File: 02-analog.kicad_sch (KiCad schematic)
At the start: 24 parts, among them J2 Superseal_1.0_5pol_MicA, J3 Superseal_1.0_5pol_MicB

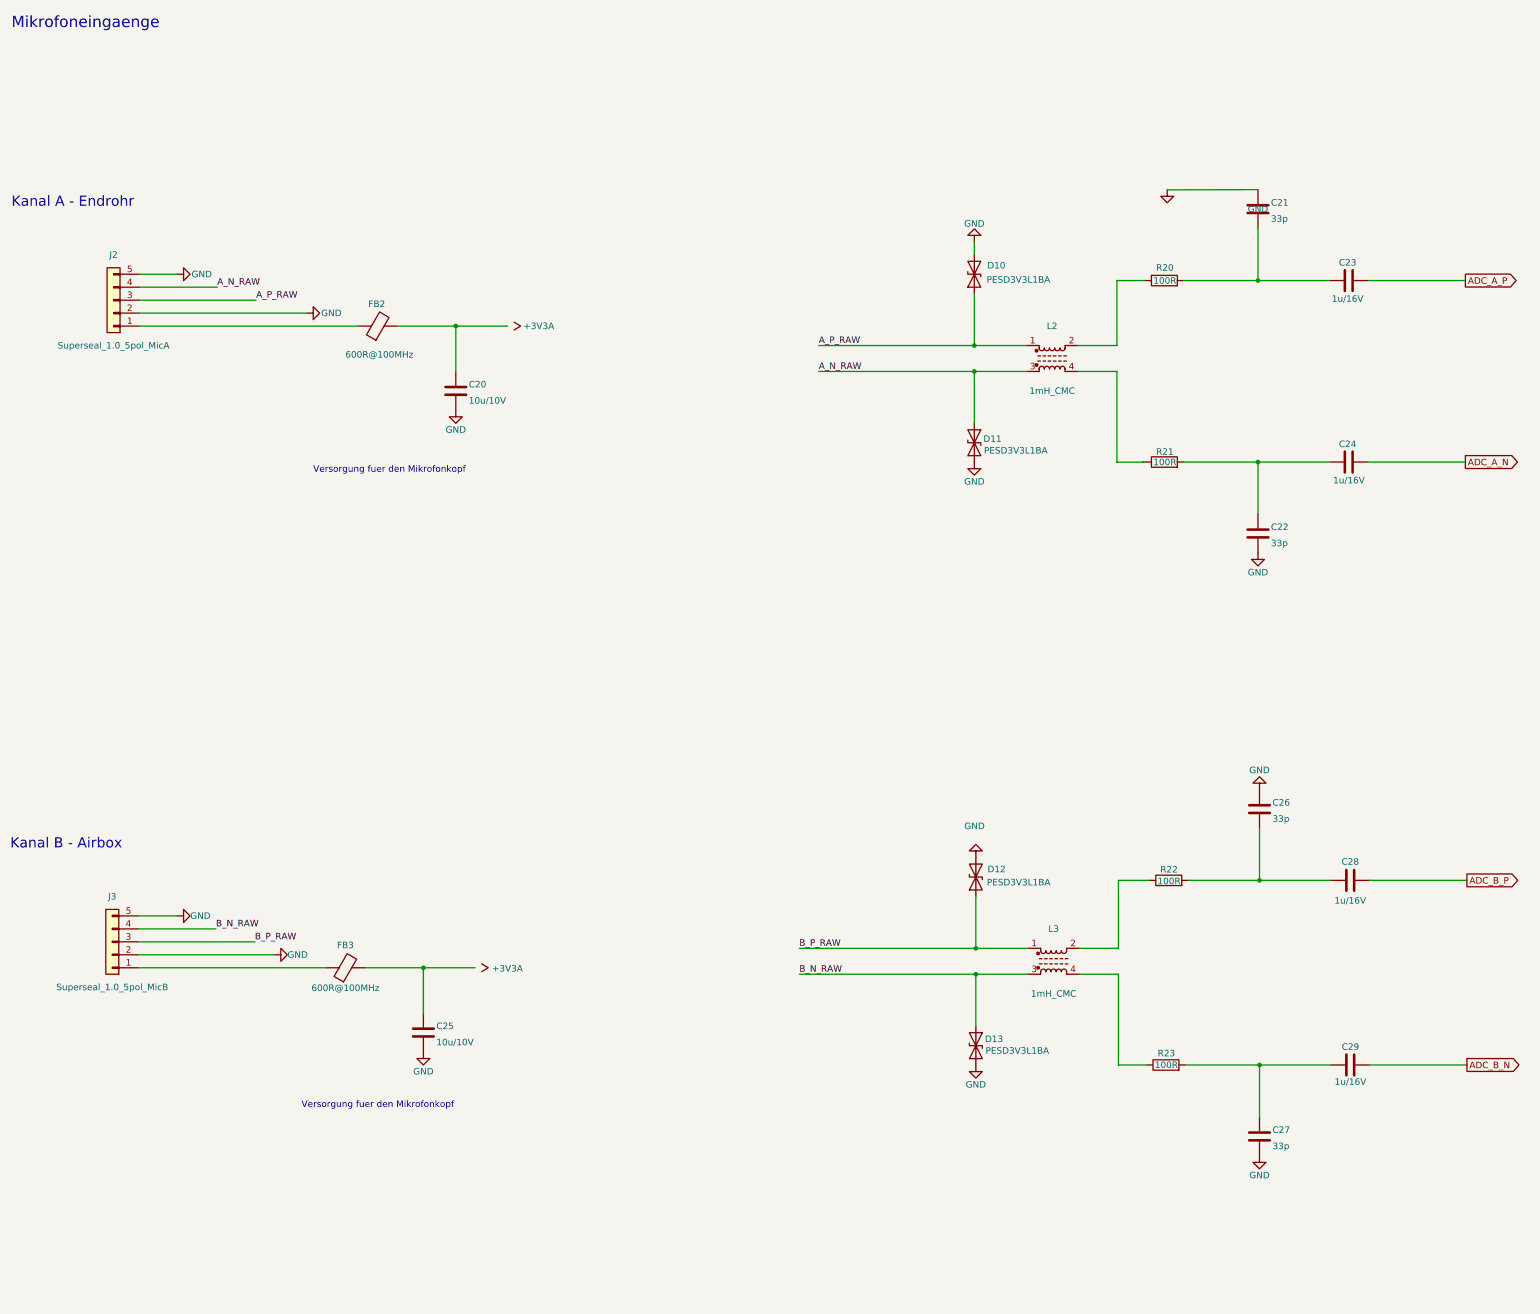
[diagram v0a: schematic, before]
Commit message: Layout verdrahten, ERC/DRC bereinigen, Werkzeugkette auf KiCad 10
Mikrofonkopf ist fertig verdrahtet (0 offene Verbindungen, 0 DRC-Fehler).
Auf der Hauptplatine bleiben 16 Verbindungen offen, ebenfalls ohne
DRC-Fehler; sie sind im interaktiven Router von KiCad zu schliessen.

Schaltplan
- 3 Speisepin-Fehler behoben (+4V6, ADC-AVDD, Uhrenbatterie brauchen ein
  Speiseflag - sie werden ueber Drossel, Ferrit bzw. Zelle gespeist und
  haben damit keine Quelle im Sinne der Regelpruefung)
- Netzname GND_CHASSIS entfernt: lag auf demselben Knoten wie GND
- TLV1117LV33 hatte einen Pin 4 fuer die Kuehlfahne, den es im Footprint
  SOT-223-3_TabPin2 nicht gibt - dort traegt Pad 2 die Fahne
- Piezo von Durchsteck- auf SMD-Ausfuehrung (Murata PKMCS0909E): fuer den
  12,5-mm-Typ gibt es keine Position, an der seine Anschluesse nicht auf
  der Gegenseite auf Pads treffen
- ERC laeuft jetzt fehlerfrei

Layout
- Durchsteckpads belegen beide Seiten. J1, J4 und J6 standen ueber
  rueckseitigen Bauteilen; das waren vier echte Kurzschluesse, unter
  anderem GPS_PPS gegen Masse an der Knopfzelle. Die eigene Pruefung
  vergleicht Durchsteckpads jetzt gegen beide Seiten, pad-genau
- In2 traegt keine Versorgungsinseln mehr, sondern Signale. Vorher wich
  der Autorouter auf die Masseflaeche aus - 140 Segmente aus 30 Netzen
  quer durch In1. Der DSN-Export kennzeichnet In1 nun als Versorgungslage
- Masseflaechen auf den Aussenlagen mit Naehvias an In1 angebunden und auf
  automatische Inselentfernung gestellt
- Netzklasse auf 0,18 mm Bahn, 0,15 mm Abstand, 0,5/0,25-mm-Via verengt;
  mit KiCads Vorgabewerten blieb rund ein Dutzend Verbindungen mehr offen
- Beschaffungsfelder unsichtbar und auf die Fab-Lage: sichtbar im
  Siebdruck ueberdecken die Herstellernummern die halbe Platine, das
  waren 151 der urspruenglich 214 Regelwarnungen

Werkzeuge
- pipeline.sh fasst den Layoutlauf zusammen
- fix_drc.py nimmt KiCads Regelpruefung als Instanz und entfernt, was sie
  beanstandet - die eigenen Abst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
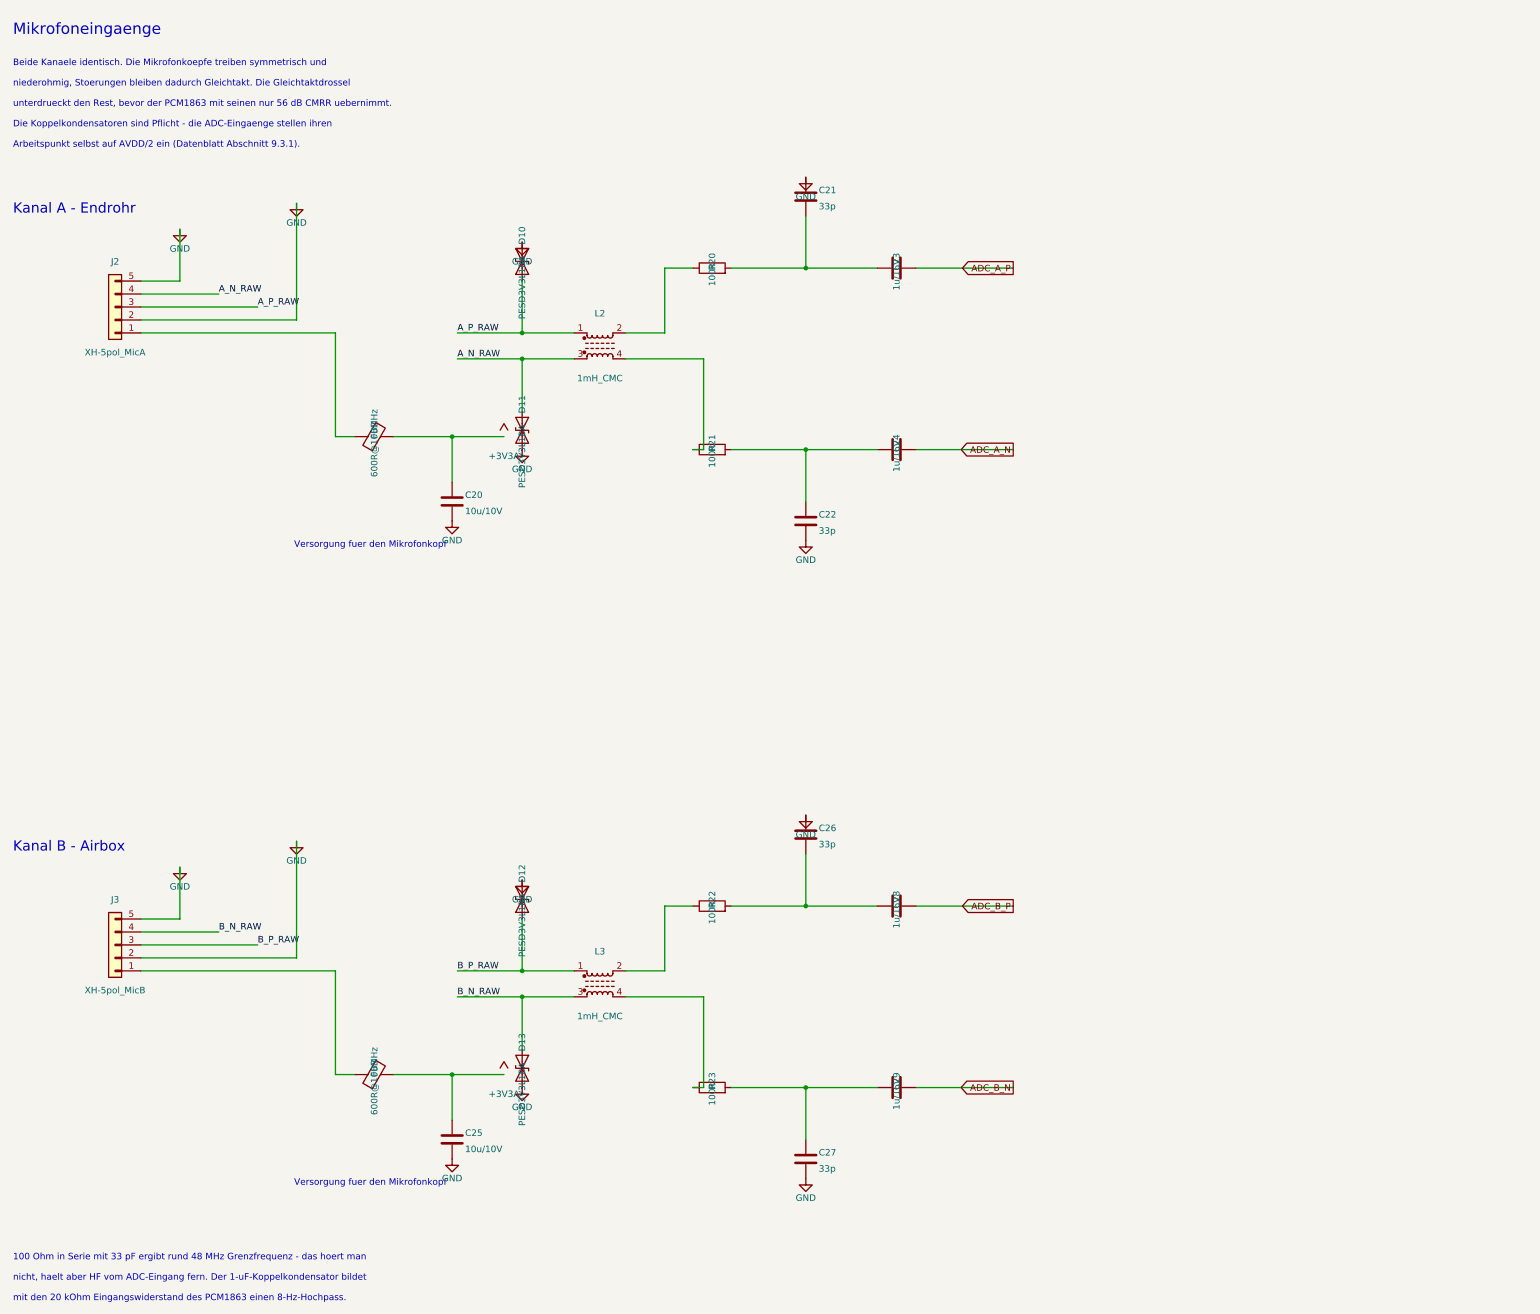
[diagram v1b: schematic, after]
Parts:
- J2: value Superseal_1.0_5pol_MicA -> XH-5pol_MicA; footprint Connector_TE:TE_Superseal_1.0_5way -> Connector_JST:JST_XH_S5B-XH-A_1x05_P2.50mm_Horizontal; MPN (none) -> S5B-XH-A(LF)(SN)
- J3: value Superseal_1.0_5pol_MicB -> XH-5pol_MicB; footprint Connector_TE:TE_Superseal_1.0_5way -> Connector_JST:JST_XH_S5B-XH-A_1x05_P2.50mm_Horizontal; MPN (none) -> S5B-XH-A(LF)(SN)
- L2, L3: footprint Inductor_SMD:L_CommonModeChoke_Wuerth_WE-SL2 -> Inductor_SMD:L_CommonMode_Wuerth_WE-SL2
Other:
- note added: "100 Ohm in Serie mit 33 pF ergibt rund 48 MHz Grenzfrequenz - das hoert man"
- note added: "Arbeitspunkt selbst auf AVDD/2 ein (Datenblatt Abschnitt 9.3.1)."
- note added: "Beide Kanaele identisch. Die Mikrofonkoepfe treiben symmetrisch und"
- note added: "Die Koppelkondensatoren sind Pflicht - die ADC-Eingaenge stellen ihren"
- note added: "mit den 20 kOhm Eingangswiderstand des PCM1863 einen 8-Hz-Hochpass."
- note added: "nicht, haelt aber HF vom ADC-Eingang fern. Der 1-uF-Koppelkondensator bildet"
- note added: "niederohmig, Stoerungen bleiben dadurch Gleichtakt. Die Gleichtaktdrossel"
- note added: "unterdrueckt den Rest, bevor der PCM1863 mit seinen nur 56 dB CMRR uebernimmt."
- company: (none) -> Hayabusa / exhaust-mic
- title: Mikrofoneingaenge, EMV-Filter, ADC-Ankopplung -> Exhaust-Mic - Mikrofoneingaenge, EMV-Filter, ADC-Ankopplung
- moved on the sheet: C20, C21, C22, C23, C24, C25, C26, C27, C28, C29, D10, D11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

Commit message: modified:   01-power.kicad_sch 	modified:   02-analog.kicad_sch 	modified:   03-adc.kicad_sch 	modified:   04-mcu.kicad_sch 	modified:   05-io.kicad_sch 	modified:   exhaust-mic.kicad_pcb 	modified:   exhaust-mic.kicad_pro 	modified:   exhaust-mic.kicad_sch 	modified:   mic-head/mic-head.kicad_pcb 	modified:   mic-head/mic-head.kicad_pro 	modified:   mic-head/mic-head.kicad_sch 	new file:   ~exhaust-mic.kicad_pro.lck
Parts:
- J2: value XH-5pol_MicA -> Superseal_1.0_5pol_MicA; footprint Connector_JST:JST_XH_S5B-XH-A_1x05_P2.50mm_Horizontal -> Connector_TE:TE_Superseal_1.0_5way; MPN S5B-XH-A(LF)(SN) -> (none)
- J3: value XH-5pol_MicB -> Superseal_1.0_5pol_MicB; footprint Connector_JST:JST_XH_S5B-XH-A_1x05_P2.50mm_Horizontal -> Connector_TE:TE_Superseal_1.0_5way; MPN S5B-XH-A(LF)(SN) -> (none)
- L2, L3: footprint Inductor_SMD:L_CommonMode_Wuerth_WE-SL2 -> Inductor_SMD:L_CommonModeChoke_Wuerth_WE-SL2
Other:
- note removed: "100 Ohm in Serie mit 33 pF ergibt rund 48 MHz Grenzfrequenz - das hoert man"
- note removed: "Arbeitspunkt selbst auf AVDD/2 ein (Datenblatt Abschnitt 9.3.1)."
- note removed: "Beide Kanaele identisch. Die Mikrofonkoepfe treiben symmetrisch und"
- note removed: "Die Koppelkondensatoren sind Pflicht - die ADC-Eingaenge stellen ihren"
- note removed: "mit den 20 kOhm Eingangswiderstand des PCM1863 einen 8-Hz-Hochpass."
- note removed: "nicht, haelt aber HF vom ADC-Eingang fern. Der 1-uF-Koppelkondensator bildet"
- note removed: "niederohmig, Stoerungen bleiben dadurch Gleichtakt. Die Gleichtaktdrossel"
- note removed: "unterdrueckt den Rest, bevor der PCM1863 mit seinen nur 56 dB CMRR uebernimmt."
- company: Hayabusa / exhaust-mic -> (none)
- title: Exhaust-Mic - Mikrofoneingaenge, EMV-Filter, ADC-Ankopplung -> Mikrofoneingaenge, EMV-Filter, ADC-Ankopplung
- moved on the sheet: C20, C21, C22, C23, C24, C25, C26, C27, C28, C29, D10, D11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

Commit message: Beschaffungsdaten aus DigiKey in die vorhandenen Schaltplaene eintragen
Die Felder MPN, Hersteller und DigiKey werden nicht mehr geraten, sondern
gegen die Produktdatenbank ermittelt und mit Lagerfilter geprueft. Grundlage
sind die Schaltplandateien, wie sie auf der Platte liegen - die Generatoren
sind inzwischen aelter und wurden nicht angefasst.

tools/pick_digikey.py prueft jeden Treffer gegen die Parameter, die DigiKey
mitliefert: Kapazitaet, Spannungsfestigkeit, Dielektrikum, Widerstandswert,
Toleranz, Belastbarkeit, Bauform. Die Stichwortsuche allein reicht nicht -
auf "10 kOhm 1% 0603" antwortet DigiKey auch mit 11,5 k in 0201. Was aus der
Schaltung kommt und nicht in der Stueckliste steht, liegt in SPEC; Mechanik
und Steckverbinder in MANUELL; nicht lagernde Typen mit Ersatz und
Begruendung in ERSATZ.

tools/apply_digikey.py schreibt die Felder in die vorhandenen Dateien, ohne
sie neu zu erzeugen: vorhandene Werte werden ersetzt, neue Felder als
Abschrift des Datenblattfelds eingefuegt, damit Einrueckung und Schreibweise
passen. Vorhandene Hinweise bleiben stehen und werden ergaenzt. Mehrteilige
Bauteile bekommen die Felder an jedem Teil.

Ergebnis: 67 von 75 Positionen mit lagernder Herstellernummer, drei
brauchen kein Bauteil. Neun Positionen weichen auf einen gleichwertigen
Ersatz aus, weil der eingetragene Typ leer ist - Begruendung steht im Feld
Hinweis am Bauteil. Offen bleiben J1/J2/J3 (Superseal 1.0 gibt es bei
DigiKey nur kabelseitig), J4 (XKB-Steckverbinder nicht gefuehrt) und MK1
(IM73A135V01 ohne Bestand, kein Ersatz mit gleichem Gehaeuse).

ERC ist unveraendert; die Stuecklisten sind neu exportiert.
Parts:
- C20, C25: DigiKey (none) -> 587-5837-1-ND; Hersteller (none) -> Taiyo Yuden; MPN (none) -> EMK212ABJ106KG-T
- C21, C22, C26, C27: DigiKey (none) -> 1276-1070-1-ND; Hersteller (none) -> Samsung Electro-Mechanics; MPN (none) -> CL10C330JB8NNNC
- C23, C24, C28, C29: DigiKey (none) -> 1276-1859-1-ND; Hersteller (none) -> Samsung Electro-Mechanics; MPN (none) -> CL10A105KA8NFNC
- D10, D11, D12, D13: DigiKey (none) -> 5399-SLPESD3V3L1BACT-ND; Hersteller (none) -> Shenzhen Slkormicro Semicon Co., Ltd.; MPN (none) -> SLPESD3V3L1BA
- FB2, FB3: DigiKey (none) -> 490-1014-1-ND; Hersteller (none) -> Murata Electronics; MPN (none) -> BLM18AG601SN1D
- L2, L3: DigiKey (none) -> 732-1474-1-ND; Hersteller (none) -> Würth Elektronik
- R20, R21, R22, R23: DigiKey (none) -> 541-100HCT-ND; Hersteller (none) -> Vishay Dale; MPN (none) -> CRCW0603100RFKEA
